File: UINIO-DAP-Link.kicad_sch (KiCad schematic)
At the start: 33 parts, among them J1 扩展板串口 & 电源输出, J2 扩展板 JTAG 输出, J3 JTAG_nTRST 跳线选择, J4 3.3V 跳线选择, J5 扩展板 SWD 输入, J6 DAPLink 固件下载接口, J7 JTAG/SWD 下载接口, U1 ME6211, U2 STM32F103C8T6, Y1 Crystal_GND24

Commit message: Update design.
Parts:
- added F1: 自恢复保险丝, Fuse:Fuse_1206_3216Metric, symbol Device:Polyfuse
- added Q1: S8550, Uinio:SOT-23-3_L2.9-W1.6-P1.90-LS2.9-BL, symbol Transistor_BJT:S8550
- added R13, R14, R15: 1.5K, Resistor_SMD:R_0603_1608Metric, symbol Device:R
- added R16: 0, Resistor_SMD:R_0603_1608Metric, symbol Device:R
- Y1: footprint Crystal:Crystal_SMD_0603-4Pin_6.0x3.5mm -> Crystal:Crystal_SMD_3225-4Pin_3.2x2.5mm
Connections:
- net _VDD_3.3V is gone; now on net 3.3V_Input: J5.8 (Pin_8)
- net GND: now also R14.2
- net USB_Data_N: now also R15.1
- net VDD_3.3V: now also Q1.1 (E), R16.1
- net VDD_5V: now also F1.2; no longer USB1.A4B9 (VBUS)
- net _JTAG_nSRST_Input: now also J5.5 (Pin_5)
- net _JTAG_nSRST_Output: no longer J5.5 (Pin_5)
- net USB_ENUM renamed USB_Enumeration
- net USB_Enumeration: now also R13.1
- new net: Q1.2 (B), R13.2, R14.1
- new net: Q1.3 (C), R15.2, R16.2
- new net: F1.1, USB1.A4B9 (VBUS)
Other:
- moved on the sheet: J3, J4, R4, R5, USB1

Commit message: Prepare Version 2.0.0.
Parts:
- removed F1: 自恢复保险丝, Fuse:Fuse_1206_3216Metric, symbol Device:Polyfuse
- removed Q1: S8550, Uinio:SOT-23-3_L2.9-W1.6-P1.90-LS2.9-BL, symbol Transistor_BJT:S8550
- removed R13, R14, R15: 1.5K, Resistor_SMD:R_0603_1608Metric, symbol Device:R
- removed R16: 0, Resistor_SMD:R_0603_1608Metric, symbol Device:R
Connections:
- net VDD_5V: now also USB1.A4B9 (VBUS)
- net USB_Enumeration: no longer names the net of U2.28 (PB15)
- no-connect marks 27 -> 28
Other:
- moved on the sheet: USB1

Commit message: Release UINIO-DAP-Link 3.0.0.
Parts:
- added R13, R14: 22R, Resistor_SMD:R_0603_1608Metric, symbol Device:R
- added R15: 1.5K, Resistor_SMD:R_0603_1608Metric, symbol Device:R
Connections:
- net USB_Data_N: now also R14.1; no longer USB1.A7 (DN1), USB1.B7 (DN2)
- net USB_Data_P: now also R13.1, R15.2; no longer USB1.A6 (DP1), USB1.B6 (DP2)
- net VDD_3.3V: now also R15.1
- new net USB_+: R13.2, USB1.A6 (DP1), USB1.B6 (DP2)
- new net USB_-: R14.2, USB1.A7 (DN1), USB1.B7 (DN2)
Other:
- moved on the sheet: USB1

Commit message: Update PCB.
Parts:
- added R16, R17: 5.1K, Resistor_SMD:R_0603_1608Metric, symbol Device:R
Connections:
- net GND: now also R16.1, R17.1
- net at USB1.A5 (CC1): now also R16.2
- net at USB1.B5 (CC2): now also R17.2
- no-connect marks 28 -> 26
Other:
- moved on the sheet: R13, R14, USB1

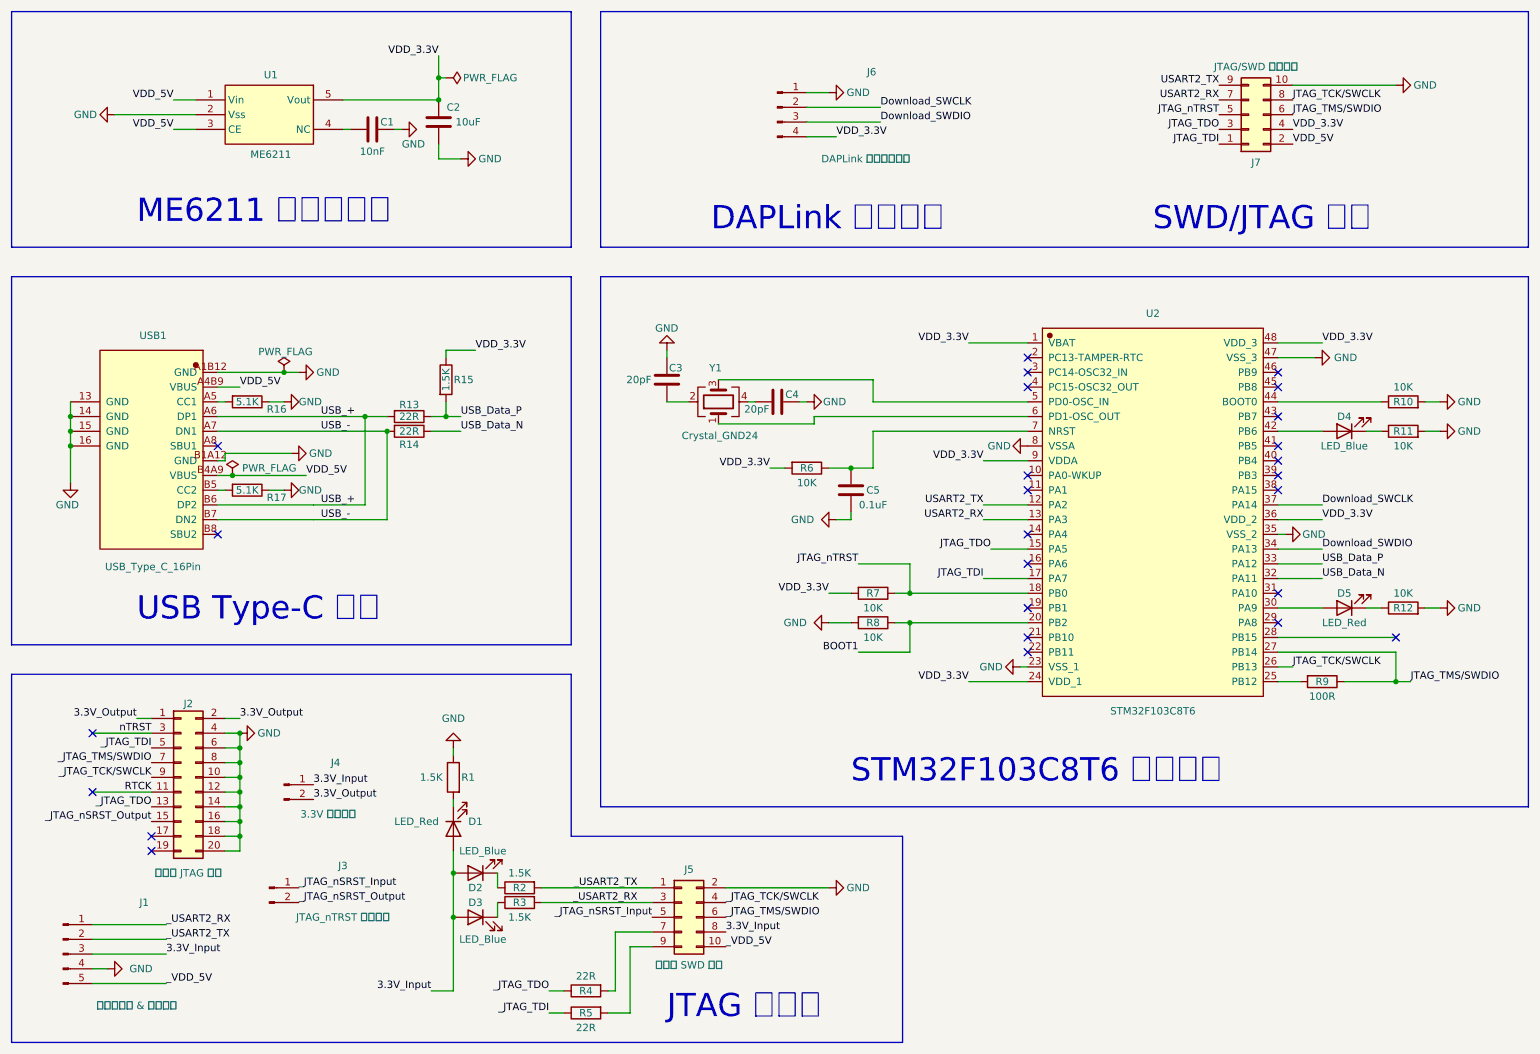
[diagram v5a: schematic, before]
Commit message: Release UINIO-DAP-Link version 3.2.0.
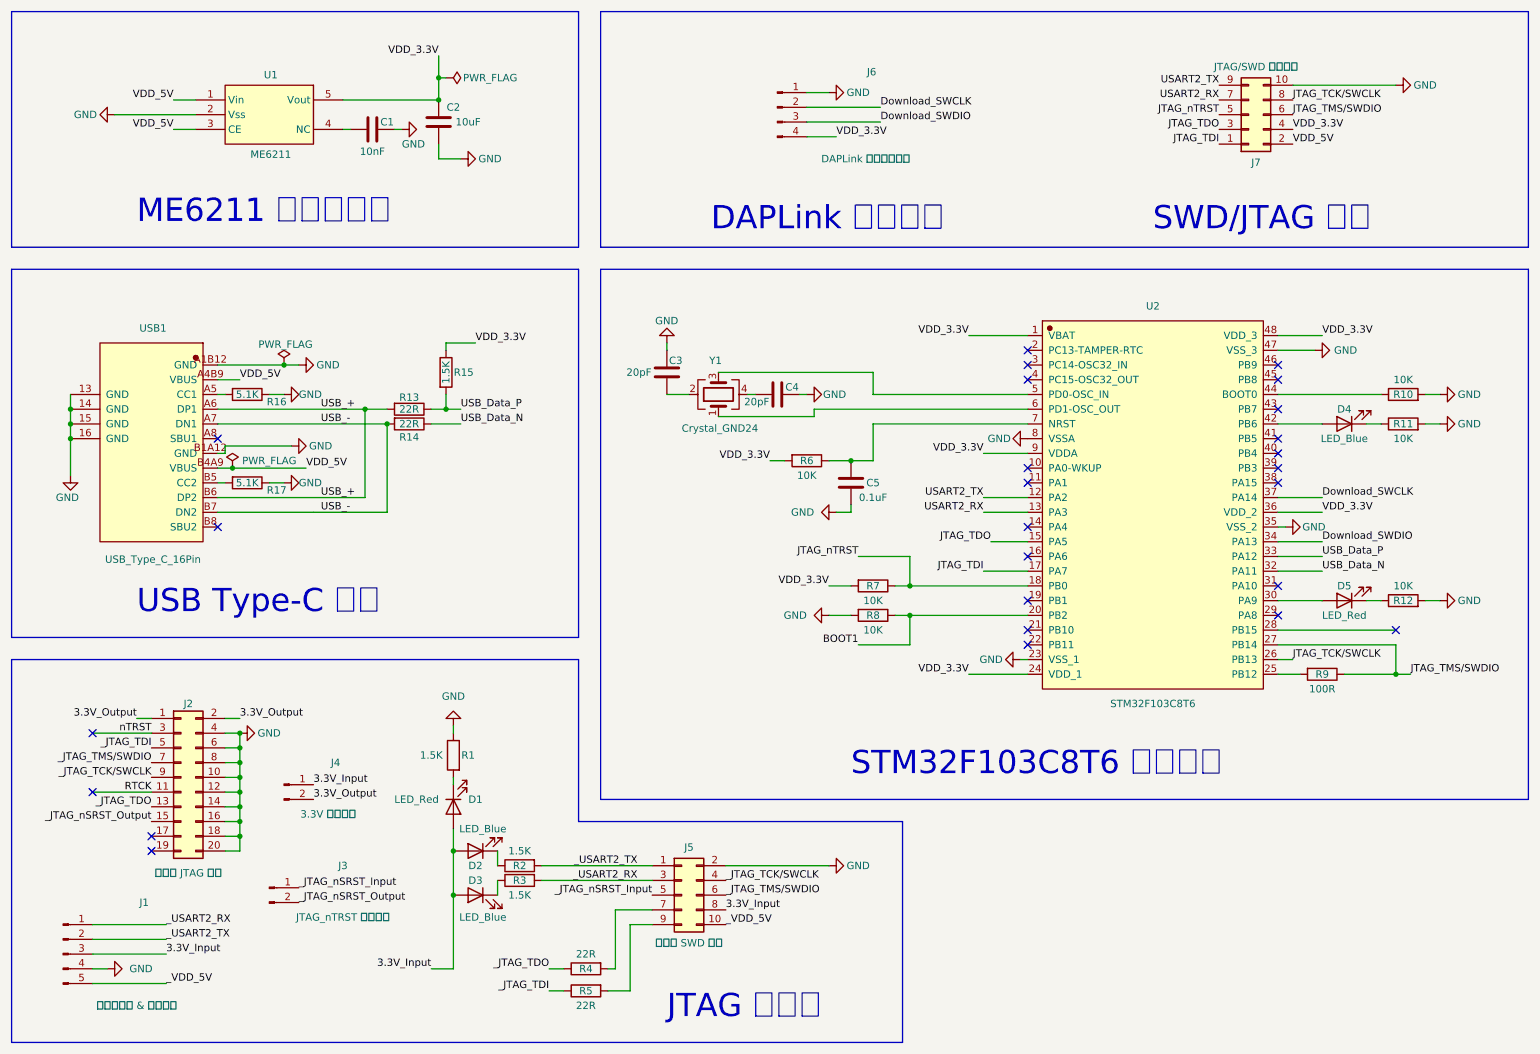
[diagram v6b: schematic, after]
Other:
- moved on the sheet: C3, C4, C5, D1, D2, D3, D4, D5, J5, R1, R10, R11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

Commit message: Prepare version 3.3.0.
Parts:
- removed J1: 扩展板串口 & 电源输出, Connector_PinHeader_2.54mm:PinHeader_1x05_P2.54mm_Vertical, symbol Connector:Conn_01x05_Male
- removed J3: JTAG_nTRST 跳线选择, Connector_PinHeader_2.54mm:PinHeader_1x02_P2.54mm_Vertical, symbol Connector:Conn_01x02_Male
- removed J4: 3.3V 跳线选择, Connector_PinHeader_2.54mm:PinHeader_1x02_P2.54mm_Vertical, symbol Connector:Conn_01x02_Male
- removed J6: DAPLink 固件下载接口, Connector_PinHeader_2.54mm:PinHeader_1x04_P2.54mm_Vertical, symbol Connector:Conn_01x04_Male
- added J1: 扩展板串口 & 电源输出, Connector_PinHeader_2.54mm:PinHeader_1x05_P2.54mm_Vertical, symbol Connector:Conn_01x05_Pin
- added J3: JTAG_nTRST 跳线选择, Connector_PinHeader_2.54mm:PinHeader_1x02_P2.54mm_Vertical, symbol Connector:Conn_01x02_Pin
- added J4: 3.3V 跳线选择, Connector_PinHeader_2.54mm:PinHeader_1x02_P2.54mm_Vertical, symbol Connector:Conn_01x02_Pin
- added J6: DAPLink 固件下载接口, Connector_PinHeader_2.54mm:PinHeader_1x04_P2.54mm_Vertical, symbol Connector:Conn_01x04_Pin
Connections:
- net 3.3V_Input: now also J1.3 (Pin_3), J4.1 (Pin_1)
- net 3.3V_Output: now also J4.2 (Pin_2)
- net Download_SWCLK: now also J6.2 (Pin_2)
- net Download_SWDIO: now also J6.3 (Pin_3)
- net GND: now also J1.4 (Pin_4), J6.1 (Pin_1)
- net VDD_3.3V: now also J6.4 (Pin_4)
- net _JTAG_nSRST_Input: now also J3.1 (Pin_1)
- net _JTAG_nSRST_Output: now also J3.2 (Pin_2)
- net _USART2_RX: now also J1.1 (Pin_1)
- net _USART2_TX: now also J1.2 (Pin_2)
- net _VDD_5V: now also J1.5 (Pin_5)

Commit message: Release UINIO-DAP-Link version 3.3.1.
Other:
- company: 电子技术博客 UinIO.com -> UinIO.com 电子技术实验室
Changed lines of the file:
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@@
   (title_block
     (title "UINIO-DAP-Link")
-    (date "2023-06-30")
-    (rev "Version 3.3.0")
-    (company "电子技术博客 UinIO.com")
+    (date "2024-01-11")
+    (rev "Version 3.3.1")
+    (company "UinIO.com 电子技术实验室")
   )
   (junction (at 27.94 85.09) (diameter 0) (color 0 0 0 0)
